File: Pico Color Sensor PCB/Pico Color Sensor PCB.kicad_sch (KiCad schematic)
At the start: 13 parts

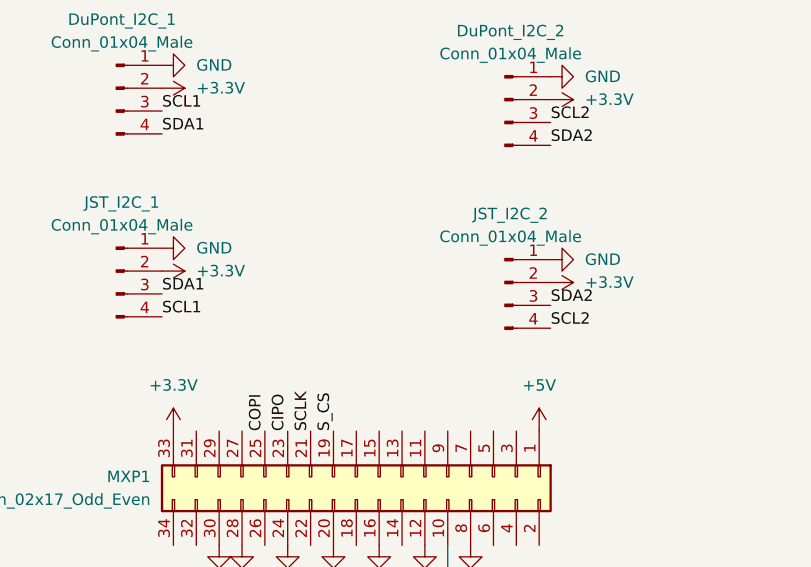
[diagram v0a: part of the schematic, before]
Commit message: Updated pinouts for JST
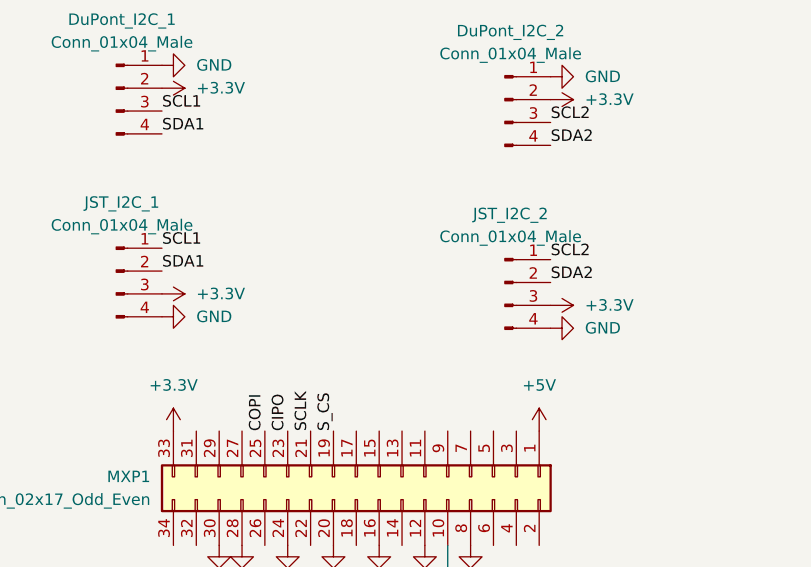
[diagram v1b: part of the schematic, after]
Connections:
- net +3.3V: now also JST_I2C_1.3 (Pin_3), JST_I2C_2.3 (Pin_3); no longer JST_I2C_1.2 (Pin_2), JST_I2C_2.2 (Pin_2)
- net GND: now also JST_I2C_1.4 (Pin_4), JST_I2C_2.4 (Pin_4); no longer JST_I2C_1.1 (Pin_1), JST_I2C_2.1 (Pin_1)
- net SCL1: now also JST_I2C_1.1 (Pin_1); no longer JST_I2C_1.4 (Pin_4)
- net SCL2: now also JST_I2C_2.1 (Pin_1); no longer JST_I2C_2.4 (Pin_4)
- net SDA1: now also JST_I2C_1.2 (Pin_2); no longer JST_I2C_1.3 (Pin_3)
- net SDA2: now also JST_I2C_2.2 (Pin_2); no longer JST_I2C_2.3 (Pin_3)
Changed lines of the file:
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@@
     (effects (font (size 1.27 1.27)) (justify left bottom))
   )
-  (label "SDA1" (at 41.91 101.6 0)
+  (label "SDA1" (at 41.91 99.06 0)
     (effects (font (size 1.27 1.27)) (justify left bottom))
   )
@@
     (effects (font (size 1.27 1.27)) (justify left bottom))
   )
-  (label "SDA2" (at 85.09 102.87 0)
+  (label "SDA2" (at 85.09 100.33 0)
     (effects (font (size 1.27 1.27)) (justify left bottom))
   )
@@
     (effects (font (size 1.27 1.27)) (justify left bottom))
   )
-  (label "SCL2" (at 85.09 105.41 0)
+  (label "SCL2" (at 85.09 97.79 0)
     (effects (font (size 1.27 1.27)) (justify left bottom))
   )
@@
     (effects (font (size 1.27 1.27)) (justify right bottom))
   )
-  (label "SCL1" (at 41.91 104.14 0)
+  (label "SCL1" (at 41.91 96.52 0)
     (effects (font (size 1.27 1.27)) (justify left bottom))
   )
@@
     (effects (font (size 1.27 1.27)) (justify left bottom))
   )
-  (symbol (lib_id "power:+3.3V") (at 85.09 100.33 270) (unit 1)
-    (in_bom yes) (on_board yes) (fields_autoplaced)
-    (property "Reference" "#PWR0115" (id 0) (at 81.28 100.33 0)
-      (effects (font (size 1.27 1.27)) hide)
-    )
-    (property "Value" "+3.3V" (id 1) (at 88.9 100.3299 90)
-      (effects (font (size 1.27 1.27)) (justify left))
-    )
-    (property "Footprint" "" (id 2) (at 85.09 100.33 0)
-      (effects (font (size 1.27 1.27)) hide)
-    )
-    (property "Datasheet" "" (id 3) (at 85.09 100.33 0)
+  (symbol (lib_id "power:+3.3V") (at 85.09 102.87 270) (unit 1)
+    (in_bom yes) (on_board yes)
+    (property "Reference" "#PWR0115" (id 0) (at 81.28 102.87 0)
+      (effects (font (size 1.27 1.27)) hide)
+    )
+    (property "Value" "+3.3V" (id 1) (at 88.9 102.8699 90)
+      (effects (font (size 1.27 1.27)) (justify left))
+    )
+    (property "Footprint" "" (id 2) (at 85.09 102.87 0)
+      (effects (font (size 1.27 1.27)) hide)
+    )
+    (property "Datasheet" "" (id 3) (at 85.09 102.87 0)
       (effects (font (size 1.27 1.27)) hide)
     )
@@
     )
   )
-  (symbol (lib_id "power:+3.3V") (at 41.91 99.06 270) (unit 1)
+  (symbol (lib_id "power:+3.3V") (at 41.91 101.6 270) (unit 1)
     (in_bom yes) (on_board yes)
-    (property "Reference" "#PWR0116" (id 0) (at 38.1 99.06 0)
-      (effects (font (size 1.27 1.27)) hide)
-    )
-    (property "Value" "+3.3V" (id 1) (at 45.72 99.0599 90)
-      (effects (font (size 1.27 1.27)) (justify left))
-    )
-    (property "Footprint" "" (id 2) (at 41.91 99.06 0)
-      (effects (font (size 1.27 1.27)) hide)
-    )
-    (property "Datasheet" "" (id 3) (at 41.91 99.06 0)
+    (property "Reference" "#PWR0116" (id 0) (at 38.1 101.6 0)
+      (effects (font (size 1.27 1.27)) hide)
+    )
+    (property "Value" "+3.3V" (id 1) (at 45.72 101.5999 90)
+      (effects (font (size 1.27 1.27)) (justify left))
+    )
+    (property "Footprint" "" (id 2) (at 41.91 101.6 0)
+      (effects (font (size 1.27 1.27)) hide)
+    )
+    (property "Datasheet" "" (id 3) (at 41.91 101.6 0)
       (effects (font (size 1.27 1.27)) hide)
     )
@@
     (pin "1")
   )
-  (symbol (lib_id "power:GND") (at 85.09 97.79 90) (mirror x) (unit 1)
-    (in_bom yes) (on_board yes) (fields_autoplaced)
-    (property "Reference" "#PWR0114" (id 0) (at 91.44 97.79 0)
-      (effects (font (size 1.27 1.27)) hide)
-    )
-    (property "Value" "GND" (id 1) (at 88.9 97.7899 90)
-      (effects (font (size 1.27 1.27)) (justify right))
-    )
-    (property "Footprint" "" (id 2) (at 85.09 97.79 0)
-      (effects (font (size 1.27 1.27)) hide)
-    )
-    (property "Datasheet" "" (id 3) (at 85.09 97.79 0)
+  (symbol (lib_id "power:GND") (at 85.09 105.41 90) (mirror x) (unit 1)
+    (in_bom yes) (on_board yes) (fields_autoplaced)
+    (property "Reference" "#PWR0114" (id 0) (at 91.44 105.41 0)
+      (effects (font (size 1.27 1.27)) hide)
+    )
+    (property "Value" "GND" (id 1) (at 88.9 105.4099 90)
+      (effects (font (size 1.27 1.27)) (justify right))
+    )
+    (property "Footprint" "" (id 2) (at 85.09 105.41 0)
+      (effects (font (size 1.27 1.27)) hide)
+    )
+    (property "Datasheet" "" (id 3) (at 85.09 105.41 0)
       (effects (font (size 1.27 1.27)) hide)
     )
@@
     (pin "1")
   )
-  (symbol (lib_id "power:GND") (at 41.91 96.52 90) (unit 1)
-    (in_bom yes) (on_board yes) (fields_autoplaced)
-    (property "Reference" "#PWR0113" (id 0) (at 48.26 96.52 0)
-      (effects (font (size 1.27 1.27)) hide)
-    )
-    (property "Value" "GND" (id 1) (at 45.72 96.5199 90)
-      (effects (font (size 1.27 1.27)) (justify right))
-    )
-    (property "Footprint" "" (id 2) (at 41.91 96.52 0)
-      (effects (font (size 1.27 1.27)) hide)
-    )
-    (property "Datasheet" "" (id 3) (at 41.91 96.52 0)
-      (effects (font (size 1.27 1.27)) hide)
-    )
+  (symbol (lib_id "power:GND") (at 41.91 104.14 90) (unit 1)
+    (in_bom yes) (on_board yes) (fields_autoplaced)
+    (property "Reference" "#PWR0113" (id 0) (at 48.26 104.14 0)
+      (effects (font (size 1.27 1.27)) hide)
+    )
+    (property "Value" "GND" (id 1) (at 45.72 104.1399 90)
+      (effects (font (size 1.27 1.27)) (justify right))
+    )
+    (property "Footprint" "" (id 2) (at 41.91 104.14 0)
+      (effects (font (size 1.27 1.27)) hide)
+    )
+    (property "Datasheet" "" (id 3) (at 41.91 104.14 0)
+      (effects (font (size 1.27 1.27)) hide)
+    )
